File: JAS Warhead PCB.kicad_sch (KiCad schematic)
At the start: 26 parts, among them J1 Conn_01x02_Socket, J10 Conn_01x02_Socket, J11 Conn_01x02_Socket, J2 Conn_01x02_Socket, J7 Conn_01x02_Socket, K1 Panasonic_ALFG1PF12, K2 Panasonic_ALFG1PF12, Q1 PN2222A, Q2 PN2222A, U4 LD1117S50TR_SOT223

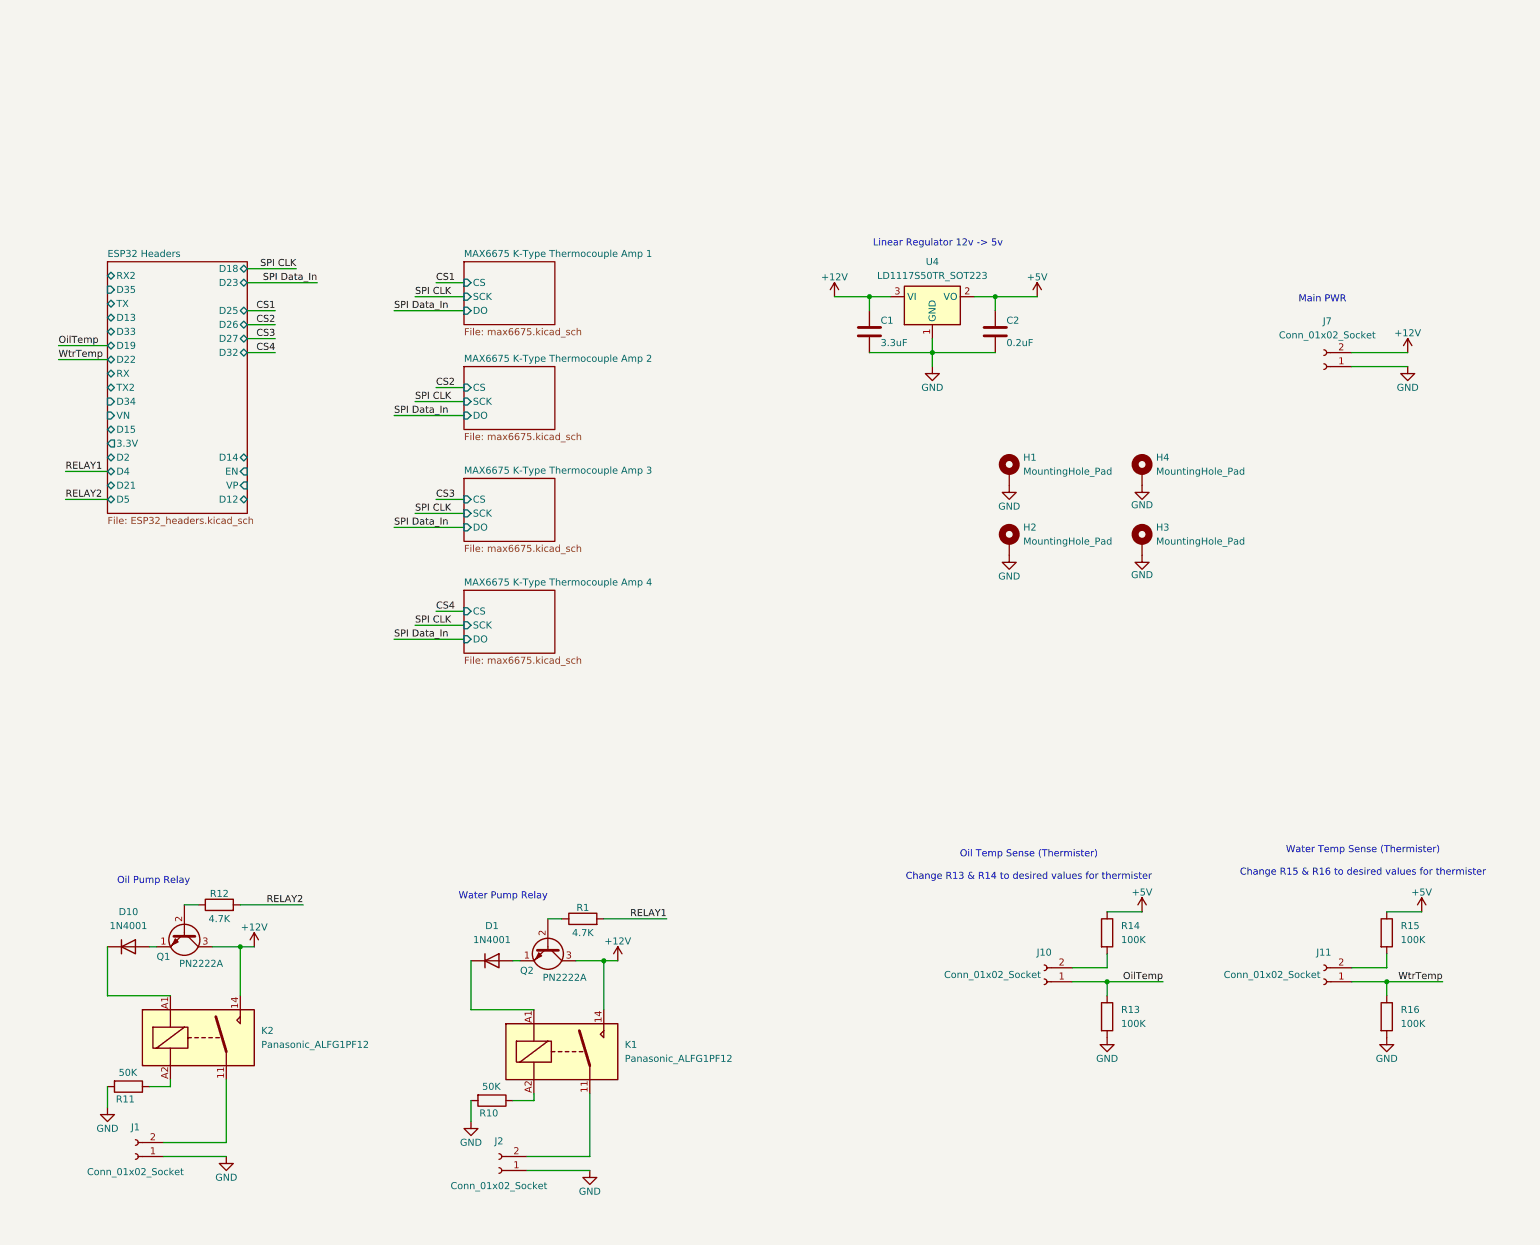
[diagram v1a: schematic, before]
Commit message: adds test & test points
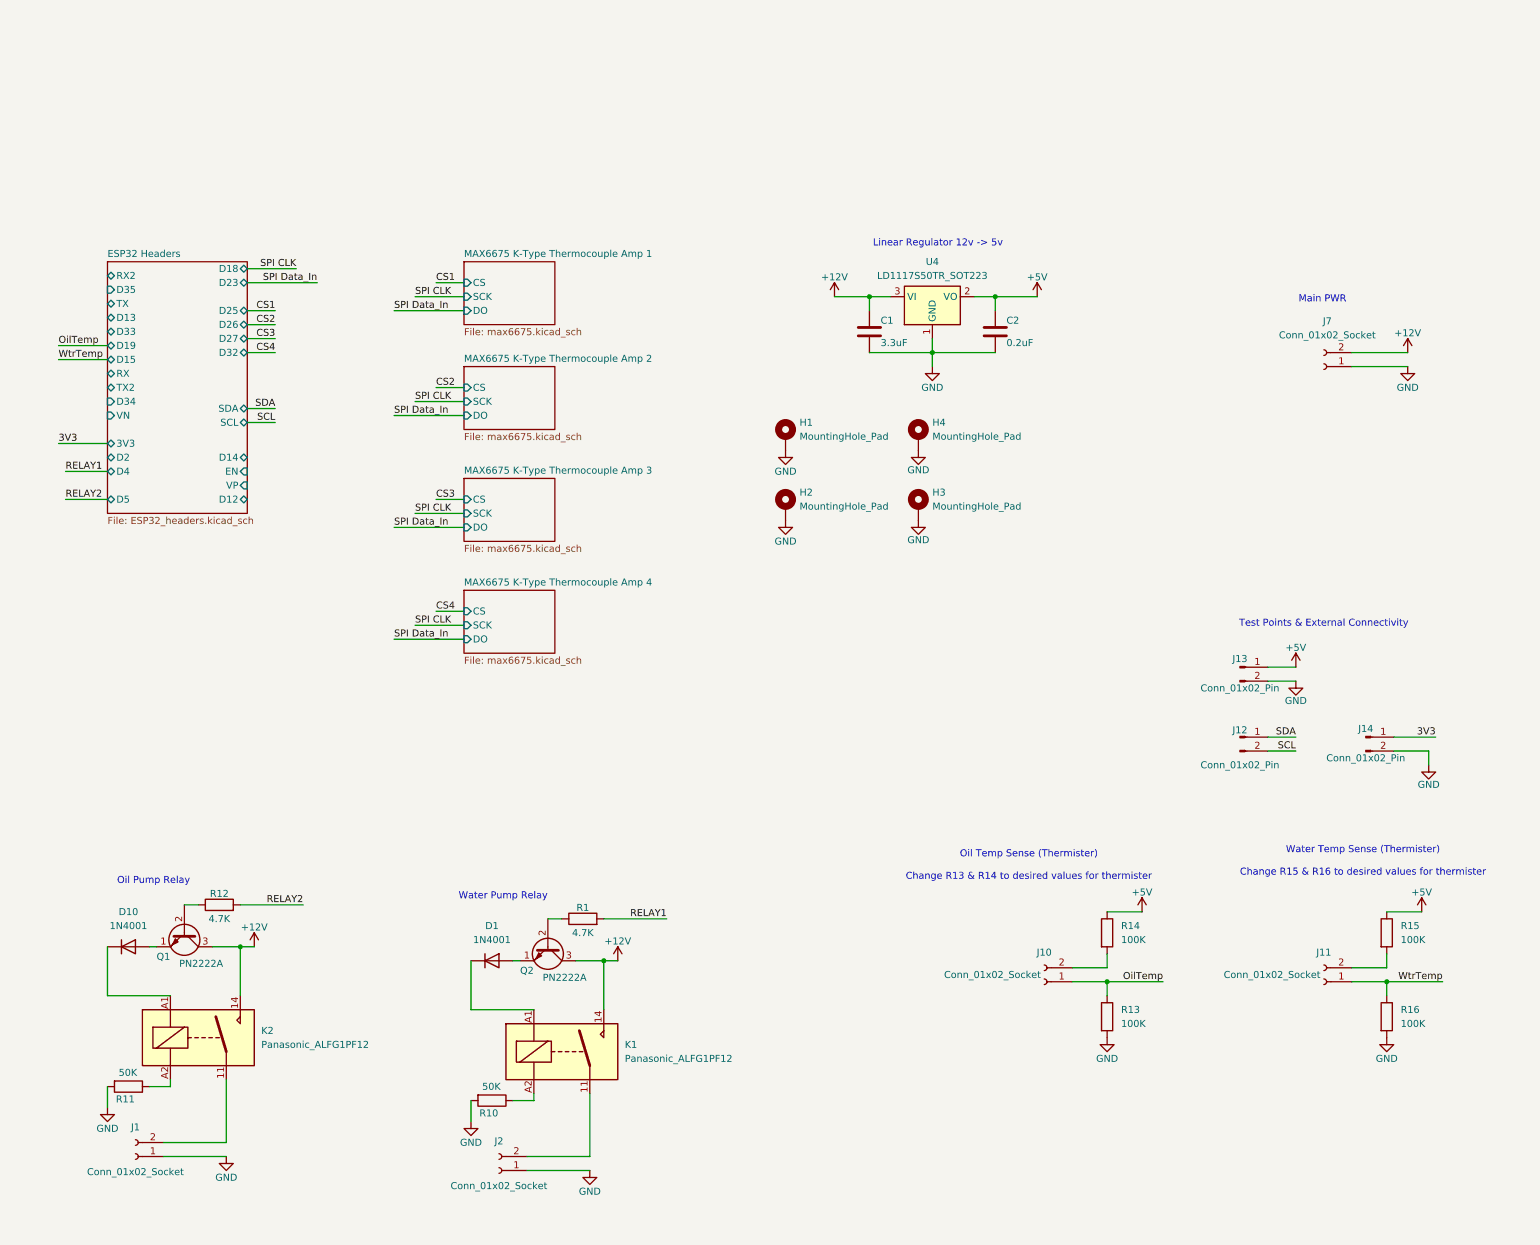
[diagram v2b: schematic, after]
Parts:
- added J12, J13, J14: Conn_01x02_Pin, Connector_PinHeader_2.54mm:PinHeader_1x02_P2.54mm_Vertical, symbol Connector:Conn_01x02_Pin
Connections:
- net +5V: now also J13.1 (Pin_1)
- net GND: now also J13.2 (Pin_2), J14.2 (Pin_2)
- new net 3V3: J14.1 (Pin_1)
- new net SCL: J12.2 (Pin_2)
- new net SDA: J12.1 (Pin_1)
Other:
- sheet ESP32 Headers ports: added 3V3, SCL, SDA; removed 3.3V, D21, D22
- note added: "Test Points & External Connectivity"
- moved on the sheet: H1, H2, H3, H4

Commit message: remove handsolder
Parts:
- R10, R11: footprint Resistor_SMD:R_2816_7142Metric_Pad3.20x4.45mm_HandSolder -> Resistor_SMD:R_2816_7142Metric
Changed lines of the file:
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@@
 			)
 		)
-		(property "Footprint" "Resistor_SMD:R_2816_7142Metric_Pad3.20x4.45mm_HandSolder"
+		(property "Footprint" "Resistor_SMD:R_2816_7142Metric"
 			(at 31.75 168.402 90)
 			(effects
@@
 			)
 		)
-		(property "Footprint" "Resistor_SMD:R_2816_7142Metric_Pad3.20x4.45mm_HandSolder"
+		(property "Footprint" "Resistor_SMD:R_2816_7142Metric"
 			(at 97.79 170.942 90)
 			(effects

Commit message: start compliance with PCBway
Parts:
- C1: Item # (none) -> 1
- C2: Item # (none) -> 2
- D1, D10: Item # (none) -> 6
- H1, H2, H3, H4: Item # (none) -> 9
- J1, J10, J11, J2, J7: footprint TerminalBlock_4Ucon:TerminalBlock_4Ucon_1x02_P3.50mm_Vertical -> TerminalBlock:TerminalBlock_bornier-2_P5.08mm; Item # (none) -> 10
- J12, J13, J14: Item # (none) -> 12
- K1, K2: Item # (none) -> 13
- Q1, Q2: Item # (none) -> 14
- R1, R12: Item # (none) -> 15
- R10, R11: Item # (none) -> 17
- R13, R14, R15, R16: Item # (none) -> 18
- U4: Item # (none) -> 20

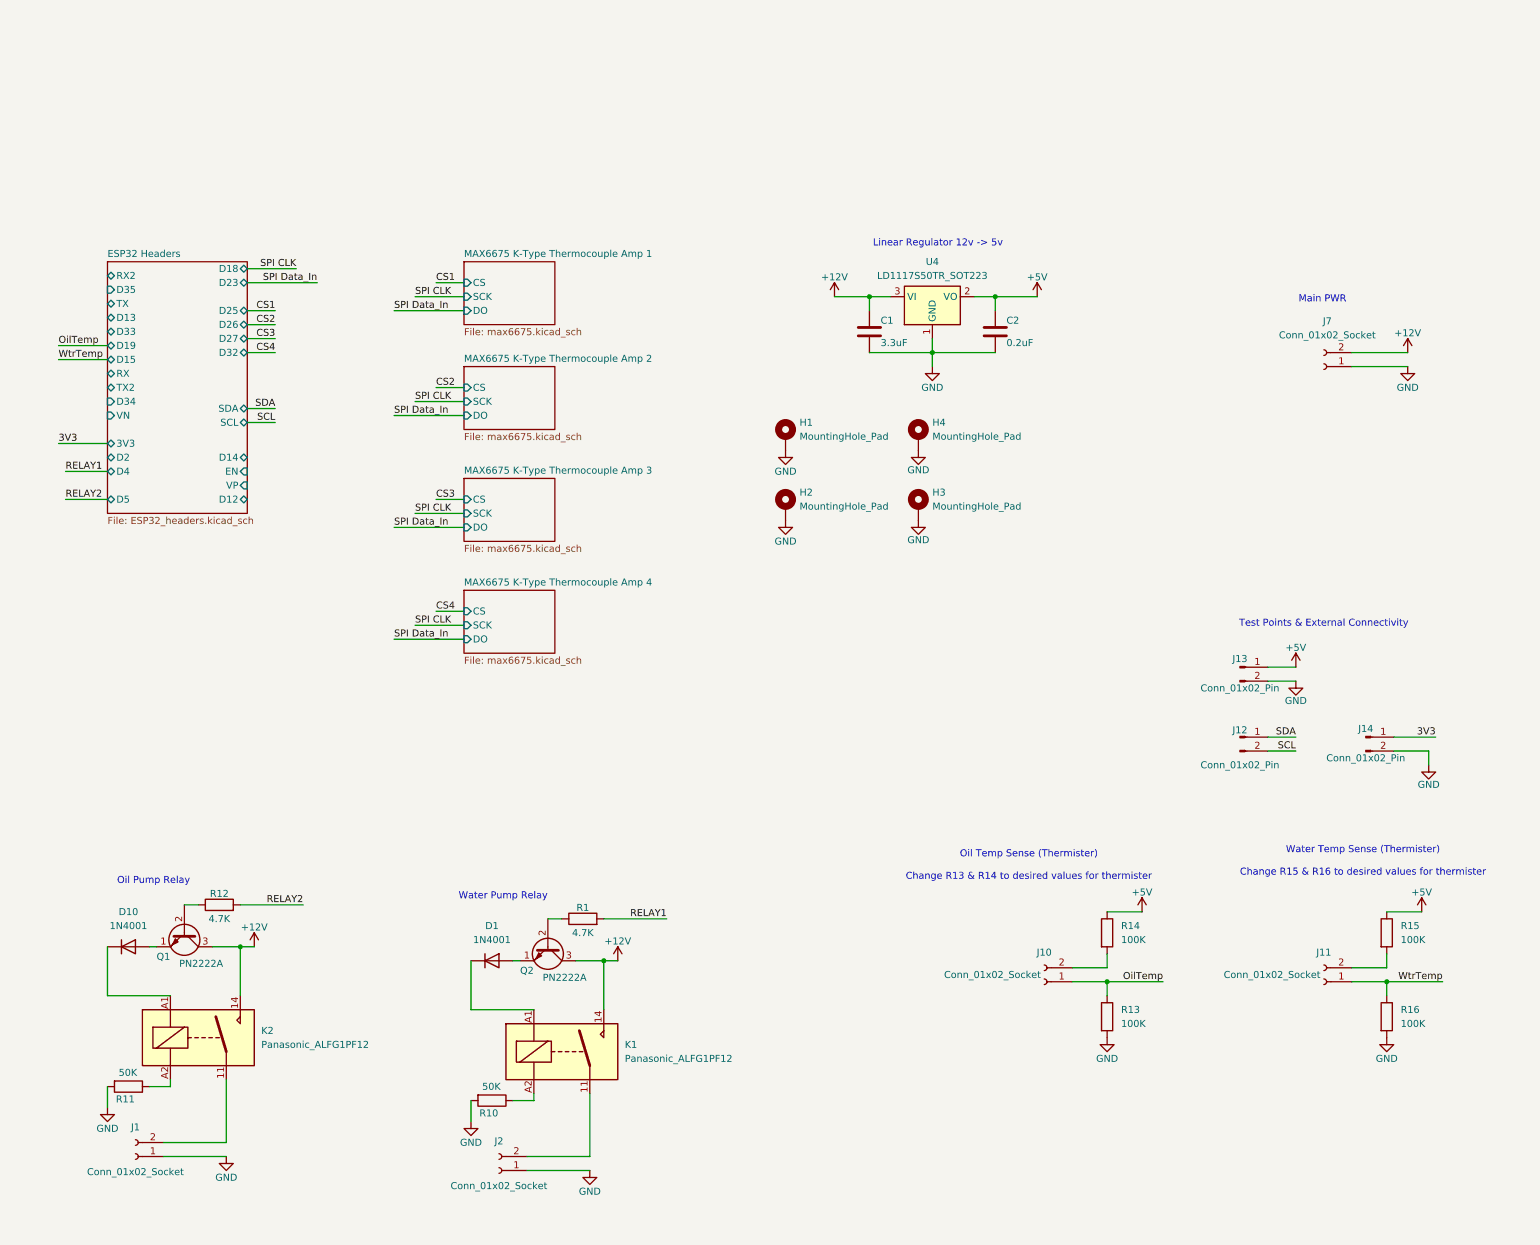
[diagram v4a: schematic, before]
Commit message: edits to conform to design regulation
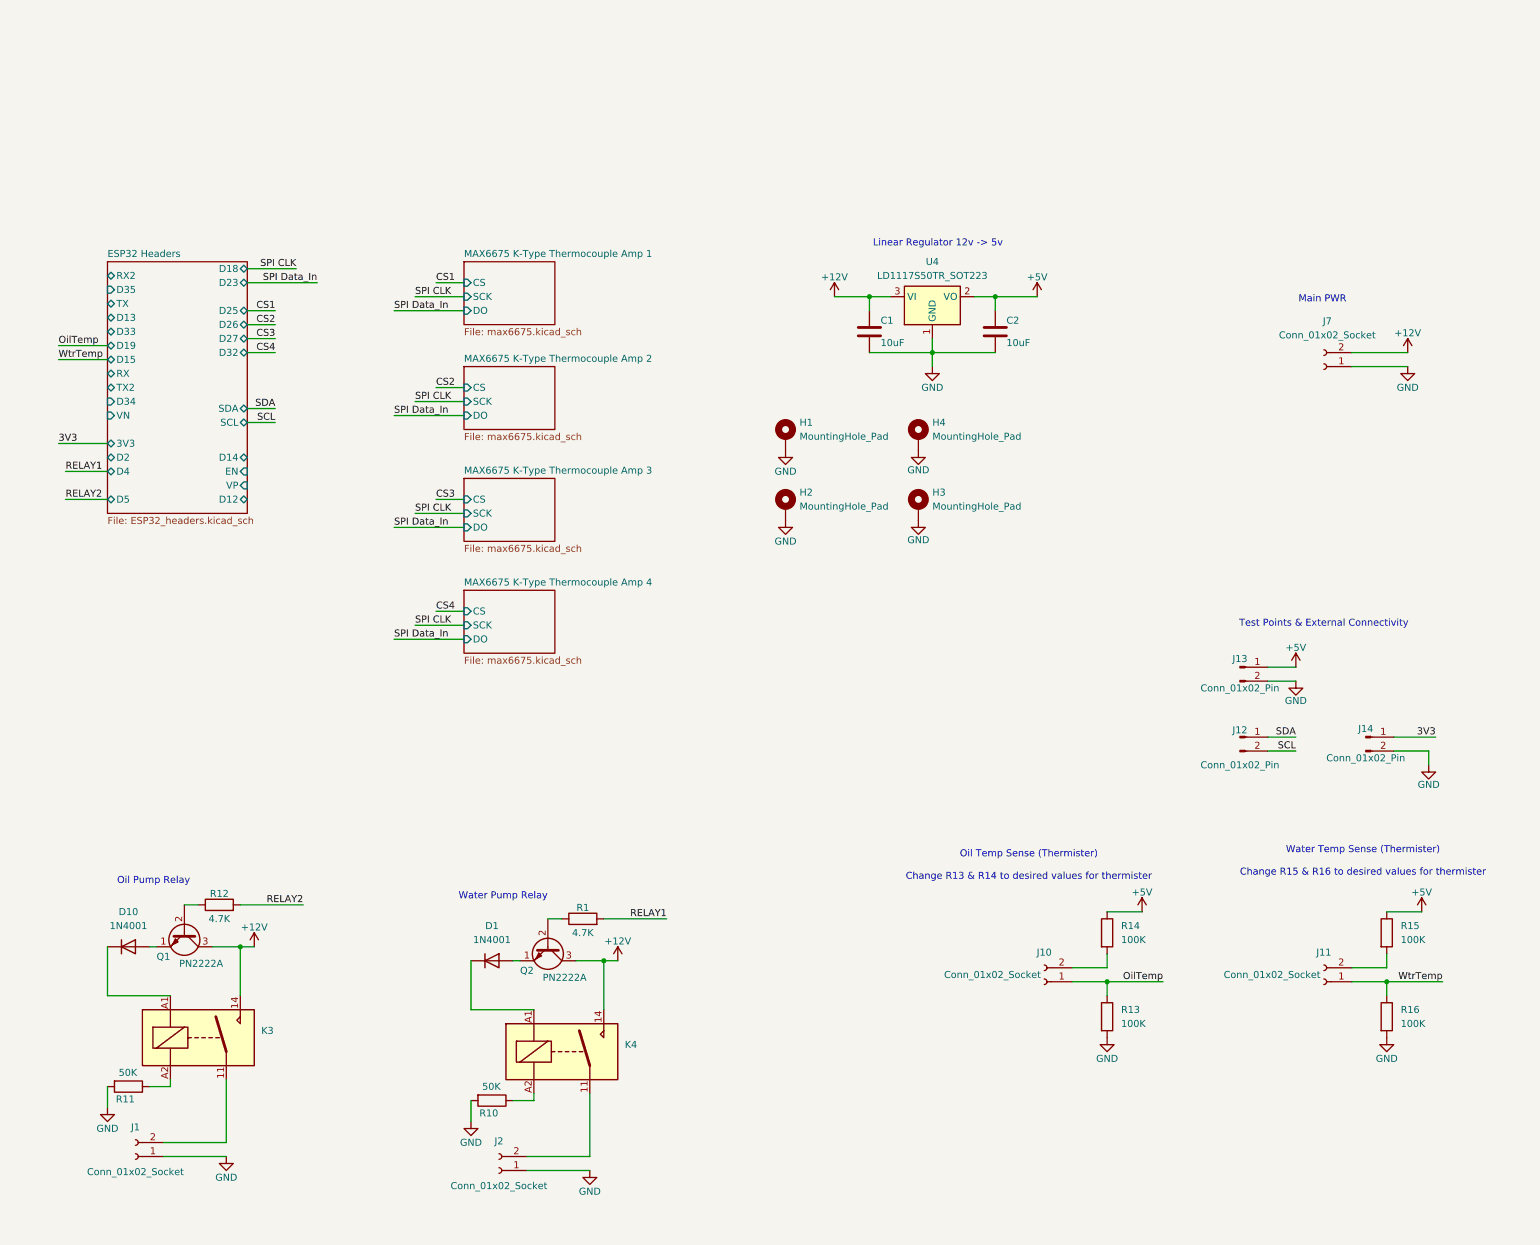
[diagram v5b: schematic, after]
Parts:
- removed K1, K2: Panasonic_ALFG1PF12, Relay_THT:Relay_SPDT_Omron_G2RL-1-E, symbol Relay:Panasonic_ALFG1PF12
- added K3, K4: Panasonic_ALFG1PF12, Relay_THT:Relay_SPST_Panasonic_ALFG_FormA_CircularHoles, symbol Relay:Panasonic_ALFG1PF12
- C1: value 3.3uF -> 10uF; footprint Capacitor_SMD:C_0504_1310Metric -> Capacitor_SMD:C_0805_2012Metric
- C2: value 0.2uF -> 10uF
- R10, R11: footprint Resistor_SMD:R_2816_7142Metric -> Resistor_SMD:R_0603_1608Metric
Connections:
- net +12V: now also K3.14, K4.14
- net at J2.2 (Pin_2): now also K4.11
- net at D10.1 (K): now also K3.A1
- net at J1.2 (Pin_2): now also K3.11
- net at R11.1: now also K3.A2
- net at D1.1 (K): now also K4.A1
- net at R10.1: now also K4.A2

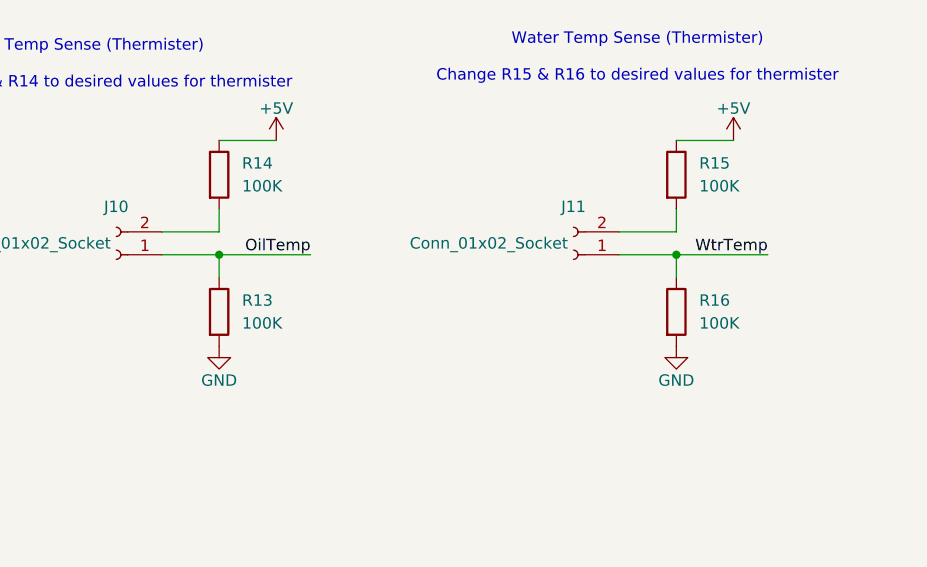
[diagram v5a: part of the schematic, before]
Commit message: change resistors
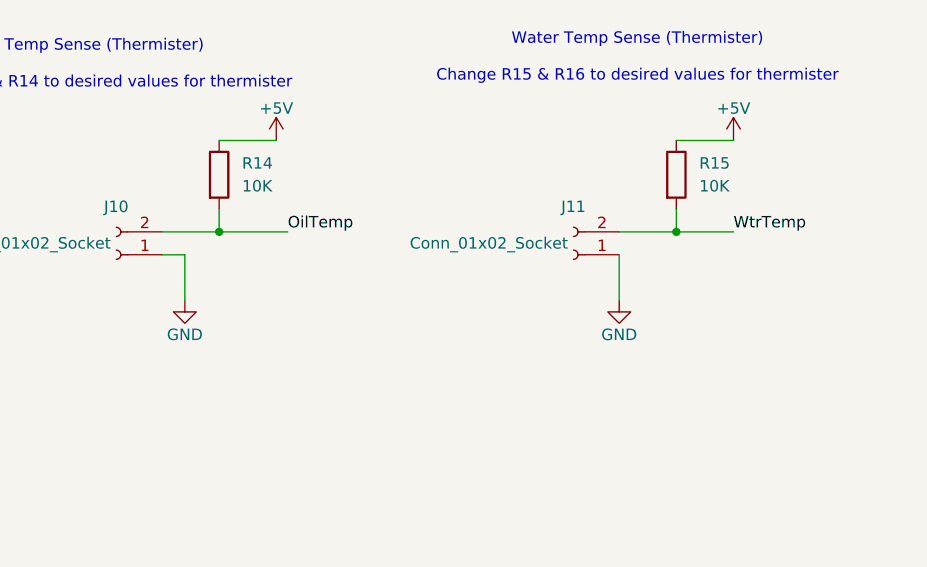
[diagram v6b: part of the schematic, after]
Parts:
- removed R13, R16: 100K, Resistor_SMD:R_0603_1608Metric, symbol Device:R
- R10, R11: footprint Resistor_SMD:R_0603_1608Metric -> Resistor_THT:R_Axial_DIN0207_L6.3mm_D2.5mm_P10.16mm_Horizontal
- R14, R15: value 100K -> 10K; footprint Resistor_SMD:R_0603_1608Metric -> Resistor_THT:R_Axial_DIN0207_L6.3mm_D2.5mm_P10.16mm_Horizontal
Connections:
- net GND: now also J10.1 (Pin_1), J11.1 (Pin_1)
- net OilTemp: now also J10.2 (Pin_2), R14.2; no longer J10.1 (Pin_1)
- net WtrTemp: now also J11.2 (Pin_2), R15.2; no longer J11.1 (Pin_1)
